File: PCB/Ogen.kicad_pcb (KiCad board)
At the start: 2 copper layers, 28 x 21.5 mm, 17 parts, among them J1 Input, U1 PMW3360DM-T2QU, U2 TLV70019, U3 TXS0102DCU, U4 TXS0102DCU, U5 TXS0102DCU

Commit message: V1.0 Lite initial commit.
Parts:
- removed U3, U4, U5: TXS0102DCU, Package_SO:VSSOP-8_2.3x2mm_P0.5mm
- added R4: 10k, Resistor_SMD:R_0402_1005Metric, B.Cu at (36.5, 18.5)
- added R5: 15k, Resistor_SMD:R_0402_1005Metric, B.Cu at (34.9, 16.7)
- A1: footprint Ogen:Ariamelon_Logo -> Ogen:Ariamelon_Logo-CU
- C1: value 4.7uF -> 1u; footprint Capacitor_SMD:C_0603_1608Metric -> Capacitor_SMD:C_0402_1005Metric; moved to B.Cu
- C2: value 100nF -> 4u7; moved to B.Cu
- C3: value 1uF -> 100n; footprint Capacitor_SMD:C_0603_1608Metric -> Capacitor_SMD:C_0402_1005Metric; moved to B.Cu
- C4: value 1uF -> 1u; footprint Capacitor_SMD:C_0603_1608Metric -> Capacitor_SMD:C_0402_1005Metric; moved to B.Cu
- H1, H2, U1: moved to B.Cu
- J1: footprint Connector_PinHeader_2.54mm:PinHeader_1x08_P2.54mm_Vertical -> Ogen:PinHeader_1x08_P2.54mm_Vertical; moved to B.Cu
- JP1: value Jumper -> MISO_Pullup; moved to B.Cu
- R1: footprint Resistor_SMD:R_0603_1608Metric -> Resistor_SMD:R_0402_1005Metric; moved to B.Cu
- R2: value 10k -> 39; footprint Resistor_SMD:R_0603_1608Metric -> Resistor_SMD:R_0402_1005Metric; moved to B.Cu
- R3: value 39R -> 10k; footprint Resistor_SMD:R_0603_1608Metric -> Resistor_SMD:R_0402_1005Metric; moved to B.Cu
- U2: value TLV70019 -> AP2127K-ADJ; moved to B.Cu
- moved H1 24.4 mm to (39.0, 24.0)
- moved H2 23.6 mm to (15.0, 24.0)
- moved U2 23.1 mm to (37.6, 16.2), turned to 180 degrees
- moved C1 19.9 mm to (40.2, 16.7), turned to 90 degrees
- moved C4 18.3 mm to (36.5, 13.9)
- moved C3 17.9 mm to (28.3, 30.7)
- moved R1 12.6 mm to (23.8, 30.7), turned to 0 degrees
- moved J1 9.32 mm to (35.9, 33.5)
- moved JP1 8.64 mm to (27.3, 14.9)
- moved A1 8.05 mm to (19.3, 15.1)
- moved C2 7.98 mm to (30.8, 30.9), turned to 0 degrees
- moved R3 7.66 mm to (30.0, 14.8)
- moved R2 6.14 mm to (30.5, 17.3), turned to 0 degrees
- moved U1 0.50 mm to (27.0, 24.0)
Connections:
- C1 pad 1: Net-(C1-Pad1) -> +3V3
- C2 pad 1: Net-(C1-Pad1) -> Net-(U1-VDDPIX)
- C3 pad 1: VCC -> GND
- C3 pad 2: GND -> Net-(U1-VDDPIX)
- C4 pad 1: VDD -> +2V
- J1 pad 1: VCC -> +3V3
- J1 pad 2: MISO-H -> /MISO
- J1 pad 3: MOSI-H -> /MOSI
- J1 pad 4: SCLK-H -> /SCK
- J1 pad 5: SS-H -> /CS
- J1 pad 6: MOT-H -> /MOTION
- J1 pad 8: NRESET-H -> /~{RST}
- JP1 pad 1: Net-(JP1-Pad1) -> Net-(JP1-A)
- JP1 pad 2: MISO -> /MISO
- R1 pad 1: NRESET -> /~{RST}
- R1 pad 2: VDD -> +3V3
- R2 pad 1: Net-(JP1-Pad1) -> Net-(U1-LED_P)
- R2 pad 2: VDD -> +2V
- R3 pad 1: Net-(R3-Pad1) -> Net-(JP1-A)
- R3 pad 2: VDD -> +3V3
- U1 pad 10: SCLK -> /SCK
- U1 pad 11: MOSI -> /MOSI
- U1 pad 12: MISO -> /MISO
- U1 pad 13: SS -> /CS
- U1 pad 15: Net-(R3-Pad1) -> Net-(U1-LED_P)
- U1 pad 3: Net-(C1-Pad1) -> Net-(U1-VDDPIX)
- U1 pad 4: VDD -> +2V
- U1 pad 5: VDD -> +3V3
- U1 pad 7: NRESET -> /~{RST}
- U1 pad 9: MOT -> /MOTION
- U2 pad 1: VCC -> +3V3
- U2 pad 3: VCC -> +3V3
- U2 pad 4: unconnected-(U2-Pad4) -> Net-(U2-ADJ)
- U2 pad 5: VDD -> +2V
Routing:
- net VDD: track 74.4 -> 0.00 mm, vias 3 -> 0
- net VCC: track 70.0 -> 0.00 mm, vias 3 -> 0
- net +3V3: track 0.00 -> 45.7 mm, vias 0 -> 3
- net SCLK-H: track 43.8 -> 0.00 mm, vias 1 -> 0
- net MOSI-H: track 36.0 -> 0.00 mm, vias 1 -> 0
- net MISO-H: track 34.3 -> 0.00 mm, vias 1 -> 0
- net +2V: track 0.00 -> 34.1 mm
- net /MOSI: track 0.00 -> 33.3 mm
- net /MISO: track 0.00 -> 32.6 mm, vias 0 -> 1
- net SS-H: track 32.2 -> 0.00 mm, vias 1 -> 0
- net /CS: track 0.00 -> 31.8 mm
- net /SCK: track 0.00 -> 27.7 mm
- net /MOTION: track 0.00 -> 21.8 mm, vias 0 -> 1
- net MOT-H: track 16.0 -> 0.00 mm, vias 2 -> 0
- net MOT: track 12.8 -> 0.00 mm
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- removed copper zone on B.Cu, net GND
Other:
- board text added: "CS"
- board text added: "Ogen V1.2"
- board text added: "RST"
- board text removed: "MISO Pullup"
- board text removed: "Ogen V1.1"
- board text removed: "RES"
- board text removed: "SS"

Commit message: Update README.md    f
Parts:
- A1: moved to F.Cu
- turned A1 to 0 degrees

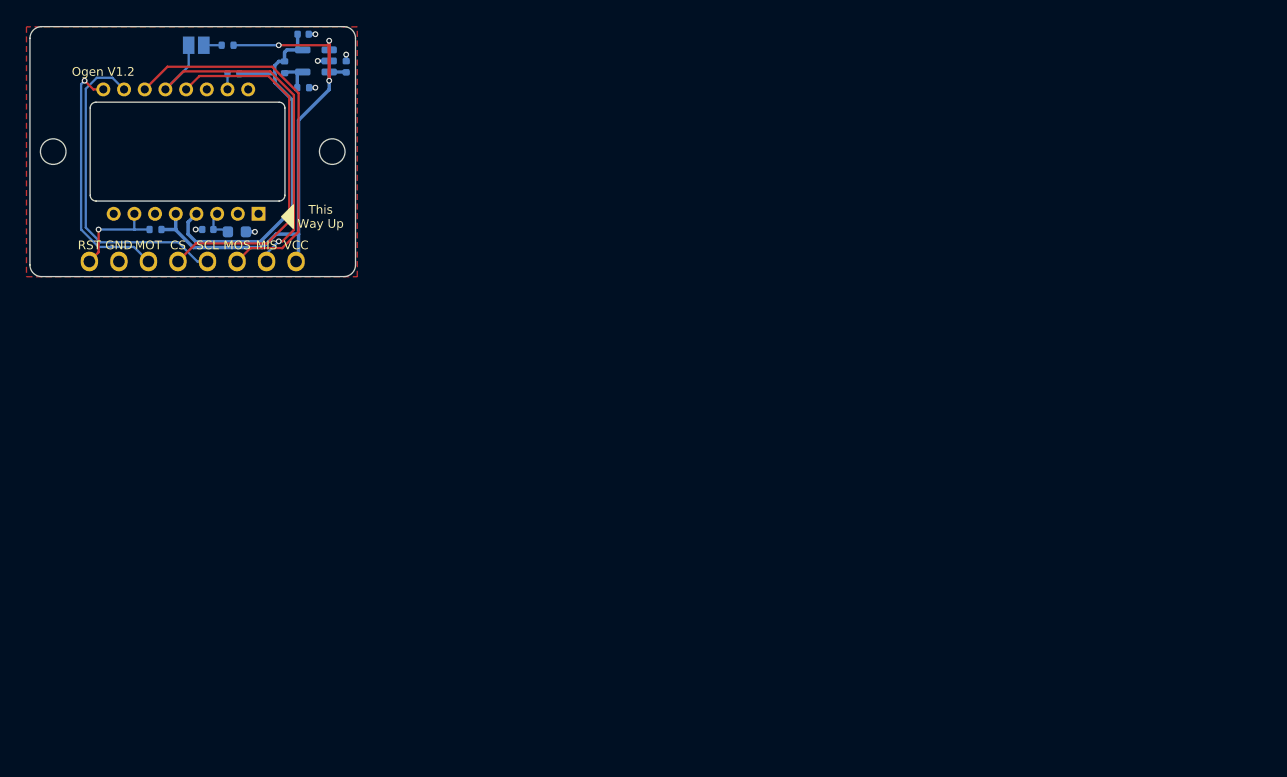
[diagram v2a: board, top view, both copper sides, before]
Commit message: 04/08/2023 update
Updated to V1.1. Changed capacitors and resistors to 0603. Stitched ground planes together. Removed MISO pullup jumper (MISO is pulled up by default now). Added metadata to schematic and PCB file. Changed location of production files for easier access.
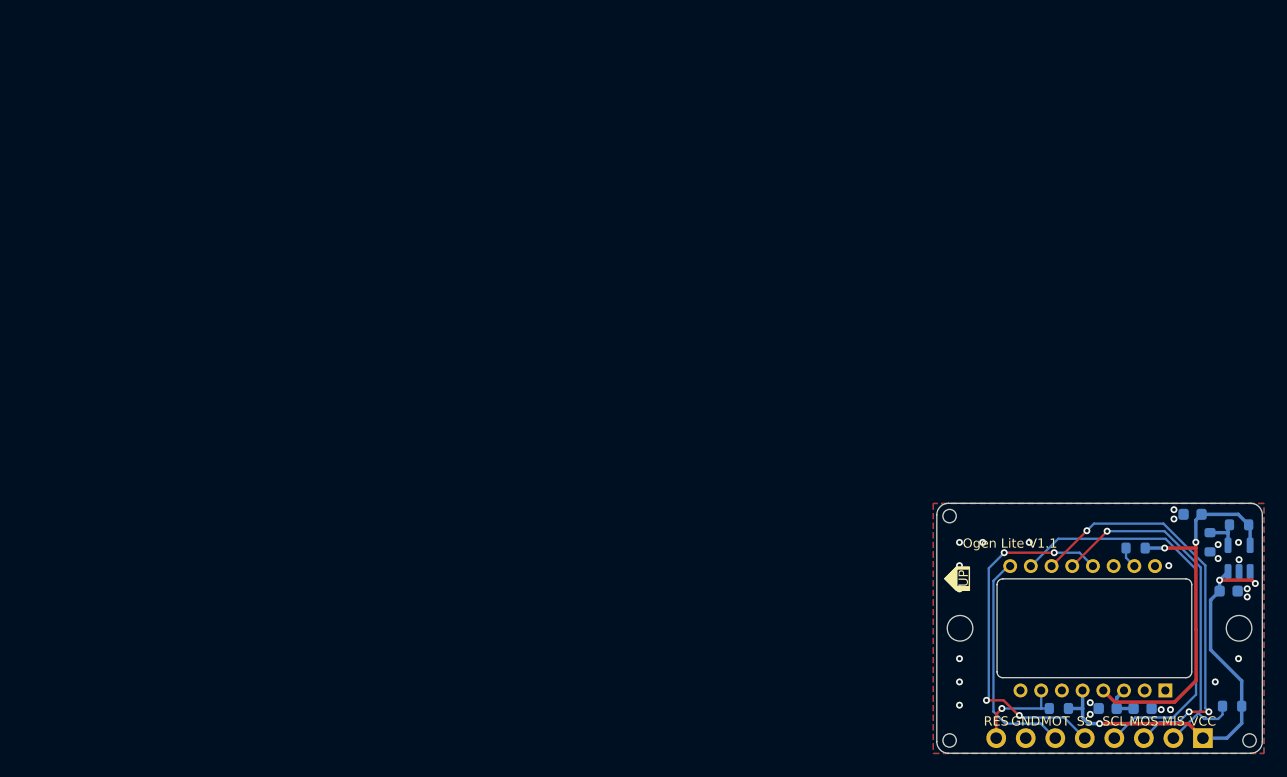
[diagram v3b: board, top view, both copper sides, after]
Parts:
- removed JP1: MISO_Pullup, Jumper:SolderJumper-2_P1.3mm_Open_Pad1.0x1.5mm
- added H3: Tooling Hole, Ogen:JLC Tooling Hole, F.Cu at (92.1, 55.4)
- added H4: Tooling Hole, Ogen:JLC Tooling Hole, F.Cu at (92.1, 74.7)
- added H5: Tooling Hole, Ogen:JLC Tooling Hole, F.Cu at (117.9, 74.7)
- C1: value 1u -> 4u7; footprint Capacitor_SMD:C_0402_1005Metric -> Capacitor_SMD:C_0603_1608Metric
- C2: value 4u7 -> 100n
- C3: value 100n -> 1u; footprint Capacitor_SMD:C_0402_1005Metric -> Capacitor_SMD:C_0603_1608Metric
- C4: footprint Capacitor_SMD:C_0402_1005Metric -> Capacitor_SMD:C_0603_1608Metric
- J1: footprint Ogen:PinHeader_1x08_P2.54mm_Vertical -> Connector_PinHeader_2.54mm:PinHeader_1x08_P2.54mm_Vertical
- R1, R4, R5: footprint Resistor_SMD:R_0402_1005Metric -> Resistor_SMD:R_0603_1608Metric
- R2: value 39 -> 10k; footprint Resistor_SMD:R_0402_1005Metric -> Resistor_SMD:R_0603_1608Metric
- R3: value 10k -> 39; footprint Resistor_SMD:R_0402_1005Metric -> Resistor_SMD:R_0603_1608Metric
- moved R2 101.7 mm to (116.4, 71.7), turned to 180 degrees
- moved C3 93.1 mm to (116.1, 61.8)
- moved R5 91.0 mm to (117.0, 56.1), turned to 180 degrees
- moved U2 90.2 mm to (117.0, 59.0), turned to 90 degrees
- moved R3 89.3 mm to (108.1, 58.1)
- moved H2 88.1 mm to (93.0, 65.0)
- moved U1 88.1 mm to (105.0, 65.0)
- moved H1 88.1 mm to (117.0, 65.0)
- moved A1 88.0 mm to (97.3, 55.8)
- moved C1 88.0 mm to (108.7, 71.9), turned to 0 degrees
- moved R1 87.9 mm to (101.5, 71.9)
- moved R4 87.3 mm to (114.5, 57.6), turned to -90 degrees
- moved C4 86.9 mm to (113.0, 55.2), turned to 180 degrees
- moved C2 85.4 mm to (105.7, 71.9)
- moved J1 80.4 mm to (105.0, 74.5)
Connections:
- net /CS renamed SS
- net /MOSI renamed MOSI
- net /MOTION renamed MOT
- net /SCK renamed SCLK
- net /~{RST} renamed NRESET
- C1 pad 1: +3V3 -> Net-(U1-VDDPIX)
- C2 pad 1: Net-(U1-VDDPIX) -> GND
- C2 pad 2: GND -> Net-(U1-VDDPIX)
- C3 pad 1: GND -> +3V3
- C3 pad 2: Net-(U1-VDDPIX) -> GND
- J1 pad 2: /MISO -> MISO
- R2 pad 1: Net-(U1-LED_P) -> +3V3
- R2 pad 2: +2V -> MISO
- R3 pad 1: Net-(JP1-A) -> Net-(U1-LED_P)
- R3 pad 2: +3V3 -> +2V
- U1 pad 12: /MISO -> MISO
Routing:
- net /MISO: track 32.6 -> 0.00 mm, vias 1 -> 0
- net MISO: track 0.00 -> 32.4 mm, vias 0 -> 1
- net +3V3: track 45.7 -> 37.7 mm
- net SCLK: track 27.7 -> 35.6 mm
- net GND: track 4.01 -> 0.00 mm, vias 6 -> 23
- net MOT: track 21.8 -> 19.5 mm, vias 1 -> 0
- net MOSI: track 33.3 -> 35.5 mm, vias 0 -> 3
- net Net-(JP1-A): track 1.54 -> 0.00 mm
- net SS: track 31.8 -> 31.2 mm, vias 0 -> 4
- net +2V: track 34.1 -> 34.3 mm, vias 0 -> 2
- added copper zone on B.Cu, net GND
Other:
- board text added: "Ogen Lite V1.1"
- board text added: "RES"
- board text added: "SS"
- board text added: "UP"
- board text removed: "CS"
- board text removed: "Ogen V1.2"
- board text removed: "RST"
- board text removed: "This Way Up"

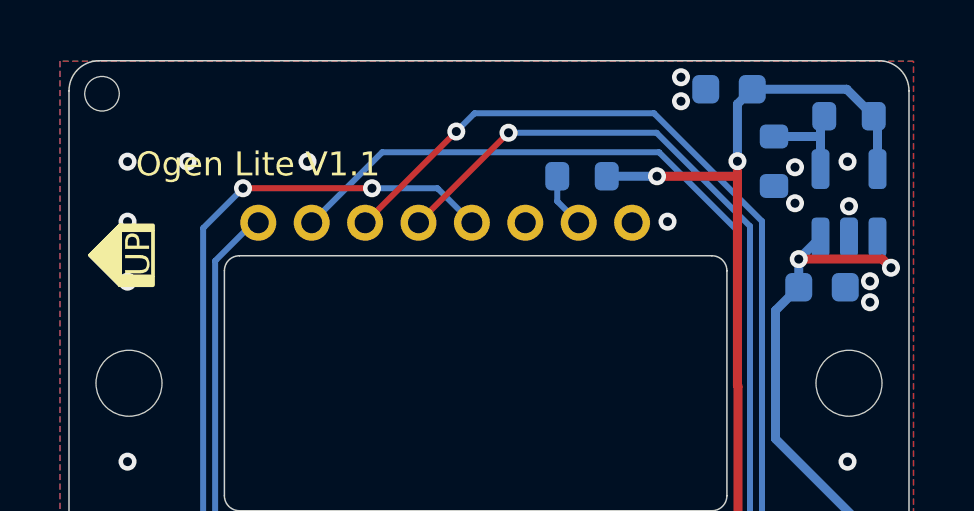
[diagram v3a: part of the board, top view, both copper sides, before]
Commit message: 18/09/2023 update
Fixed .gitignore file. Changed LDO capacitors to 4u7 to match the one used in the PMW3360.
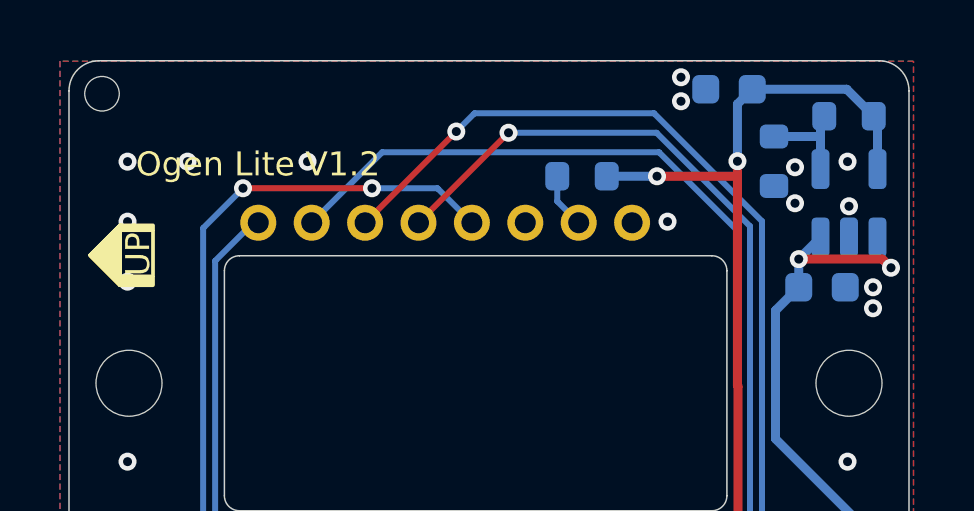
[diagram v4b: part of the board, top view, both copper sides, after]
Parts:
- C3, C4: value 1u -> 4u7
- turned C3 to 180 degrees
- turned C4 to 0 degrees
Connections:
- C3 pad 1: +3V3 -> GND
- C3 pad 2: GND -> +3V3
- C4 pad 1: +2V -> GND
- C4 pad 2: GND -> +2V
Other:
- board text added: "Ogen Lite V1.2"
- board text removed: "Ogen Lite V1.1"
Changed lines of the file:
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@@
   (title_block
     (title "Ogen Lite PMW3360 Module")
-    (date "2023-08-04")
-    (rev "V1.1")
+    (date "2023-09-18")
+    (rev "V1.2")
     (company "Created by Ariamelon (https://github.com/Ariamelon/Ogen/)")
     (comment 1 "Licensed under CC BY 4.0.")
@@
   )
   (footprint "Capacitor_SMD:C_0603_1608Metric" (layer "B.Cu")
-    (at 116.1 61.8)
+    (at 116.1 61.8 180)
     (descr "Capacitor SMD 0603 (1608 Metric), square (rectangular) end terminal, IPC_7351 nominal, (Body size source: IPC-SM-782 page 76, https://www.pcb-3d.com/wordpress/wp-content/uploads/ipc-sm-782a_amendment_1_and_2.pdf), generated with kicad-footprint-generator")
     (tags "capacitor")
     (property "Description" "0603 capacitor")
-    (property "LCSC" "C15849")
-    (property "Sheetfile" "Ogen.kicad_sch")
-    (property "Sheetname" "")
+    (property "LCSC" "C19666")
+    (property "Sheetfile" "Ogen.kicad_sch")
+    (property "Sheetname" "")
+    (property "Voltage" "16V")
     (property "ki_description" "Unpolarized capacitor, small symbol")
     (property "ki_keywords" "capacitor cap")
@@
         (effects (font (size 0.8 0.8) (thickness 0.1)) (justify mirror))
     )
-    (fp_text value "1u" (at 0 -1.43 180 unlocked) (layer "B.Fab")
-        (effects (font (size 1 1) (thickness 0.15)) (justify mirror))
-    )
-    (fp_text user "${REFERENCE}" (at 0 0 180 unlocked) (layer "B.Fab")
+    (fp_text value "4u7" (at 0 -1.43 unlocked) (layer "B.Fab")
+        (effects (font (size 1 1) (thickness 0.15)) (justify mirror))
+    )
+    (fp_text user "${REFERENCE}" (at 0 0 unlocked) (layer "B.Fab")
         (effects (font (size 1 1) (thickness 0.15)) (justify mirror))
     )
@@
     (fp_line (start 0.8 0.4) (end 0.8 -0.4)
       (stroke (width 0.1) (type solid)) (layer "B.Fab"))
-    (pad "1" smd roundrect (at -0.775 0) (size 0.9 0.95) (layers "B.Cu" "B.Paste" "B.Mask") (roundrect_rratio 0.25)
+    (pad "1" smd roundrect (at -0.775 0 180) (size 0.9 0.95) (layers "B.Cu" "B.Paste" "B.Mask") (roundrect_rratio 0.25)
+      (net 1 "GND") (pintype "passive"))
+    (pad "2" smd roundrect (at 0.775 0 180) (size 0.9 0.95) (layers "B.Cu" "B.Paste" "B.Mask") (roundrect_rratio 0.25)
       (net 3 "+3V3") (pintype "passive"))
-    (pad "2" smd roundrect (at 0.775 0) (size 0.9 0.95) (layers "B.Cu" "B.Paste" "B.Mask") (roundrect_rratio 0.25)
-      (net 1 "GND") (pintype "passive"))
     (model "${KICAD6_3DMODEL_DIR}/Capacitor_SMD.3dshapes/C_0603_1608Metric.wrl"
       (offset (xyz 0 0 0))
@@
   )
   (footprint "Capacitor_SMD:C_0603_1608Metric" (layer "B.Cu")
-    (at 113 55.2 180)
+    (at 113 55.2)
     (descr "Capacitor SMD 0603 (1608 Metric), square (rectangular) end terminal, IPC_7351 nominal, (Body size source: IPC-SM-782 page 76, https://www.pcb-3d.com/wordpress/wp-content/uploads/ipc-sm-782a_amendment_1_and_2.pdf), generated with kicad-footprint-generator")
     (tags "capacitor")
     (property "Description" "0603 capacitor")
-    (property "LCSC" "C15849")
-    (property "Sheetfile" "Ogen.kicad_sch")
-    (property "Sheetname" "")
+    (property "LCSC" "C19666")
+    (property "Sheetfile" "Ogen.kicad_sch")
+    (property "Sheetname" "")
+    (property "Voltage" "16V")
     (property "ki_description" "Unpolarized capacitor, small symbol")
     (property "ki_keywords" "capacitor cap")
     (attr smd)
-    (fp_text reference "C4" (at 2 0 unlocked) (layer "B.SilkS")
+    (fp_text reference "C4" (at -2.3 0 unlocked) (layer "B.SilkS")
         (effects (font (size 0.8 0.8) (thickness 0.1)) (justify mirror))
     )
-    (fp_text value "1u" (at 0 -1.43 unlocked) (layer "B.Fab")
-        (effects (font (size 1 1) (thickness 0.15)) (justify mirror))
-    )
-    (fp_text user "${REFERENCE}" (at 0 0 unlocked) (layer "B.Fab")
+    (fp_text value "4u7" (at 0 -1.43 -180 unlocked) (layer "B.Fab")
+        (effects (font (size 1 1) (thickness 0.15)) (justify mirror))
+    )
+    (fp_text user "${REFERENCE}" (at 0 0 -180 unlocked) (layer "B.Fab")
         (effects (font (size 1 1) (thickness 0.15)) (justify mirror))
     )
@@
     (fp_line (start 0.8 0.4) (end 0.8 -0.4)
       (stroke (width 0.1) (type solid)) (layer "B.Fab"))
-    (pad "1" smd roundrect (at -0.775 0 180) (size 0.9 0.95) (layers "B.Cu" "B.Paste" "B.Mask") (roundrect_rratio 0.25)
+    (pad "1" smd roundrect (at -0.775 0) (size 0.9 0.95) (layers "B.Cu" "B.Paste" "B.Mask") (roundrect_rratio 0.25)
+      (net 1 "GND") (pintype "passive"))
+    (pad "2" smd roundrect (at 0.775 0) (size 0.9 0.95) (layers "B.Cu" "B.Paste" "B.Mask") (roundrect_rratio 0.25)
       (net 16 "+2V") (pintype "passive"))
-    (pad "2" smd roundrect (at 0.775 0 180) (size 0.9 0.95) (layers "B.Cu" "B.Paste" "B.Mask") (roundrect_rratio 0.25)
-      (net 1 "GND") (pintype "passive"))
     (model "${KICAD6_3DMODEL_DIR}/Capacitor_SMD.3dshapes/C_0603_1608Metric.wrl"
       (offset (xyz 0 0 0))
@@
     (effects (font (size 0.8 0.8) (thickness 0.1)))
   )
-  (gr_text "Ogen Lite V1.1" (at 97.3 57.7) (layer "F.SilkS")
+  (gr_text "Ogen Lite V1.2" (at 97.3 57.7) (layer "F.SilkS")
     (effects (font (size 0.8 0.8) (thickness 0.1)))
   )
@@
   (via (at 115.2 57.8) (size 0.6) (drill 0.3) (layers "F.Cu" "B.Cu") (net 1))
   (via (at 92.951752 59.613095) (size 0.6) (drill 0.3) (layers "F.Cu" "B.Cu") (free) (net 1))
-  (via (at 117.7 62.3) (size 0.6) (drill 0.3) (layers "F.Cu" "B.Cu") (net 1))
+  (via (at 117.8 62.5) (size 0.6) (drill 0.3) (layers "F.Cu" "B.Cu") (net 1))
   (via (at 98.951752 57.613095) (size 0.6) (drill 0.3) (layers "F.Cu" "B.Cu") (free) (net 1))
   (via (at 104.2 72.4) (size 0.6) (drill 0.3) (layers "F.Cu" "B.Cu") (net 1))
@@
   (via (at 92.951752 61.613095) (size 0.6) (drill 0.3) (layers "F.Cu" "B.Cu") (free) (net 1))
   (via (at 117 59.1) (size 0.6) (drill 0.3) (layers "F.Cu" "B.Cu") (net 1))
-  (via (at 117.7 61.6) (size 0.6) (drill 0.3) (layers "F.Cu" "B.Cu") (net 1))
+  (via (at 117.8 61.8) (size 0.6) (drill 0.3) (layers "F.Cu" "B.Cu") (net 1))
   (segment (start 106.475 71.9) (end 106.475 70.975) (width 0.3) (layer "B.Cu") (net 2))
   (segment (start 106.475 70.975) (end 107.1 70.35) (width 0.3) (layer "B.Cu") (net 2))
@@
   (segment (start 116.025 56.775) (end 116.05 56.8) (width 0.3) (layer "B.Cu") (net 17))
   (zone (net 1) (net_name "GND") (layers "F&B.Cu") (hatch edge 0.508)
-    (connect_pads yes (clearance 0.2))
+    (connect_pads (clearance 0.2))
     (min_thickness 0.2) (filled_areas_thickness no)
     (fill yes (thermal_gap 0.2) (thermal_bridge_width 0.5))
